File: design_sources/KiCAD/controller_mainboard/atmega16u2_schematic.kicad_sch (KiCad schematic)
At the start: 23 parts, among them J1 02x03_pinheader, J2 01x05_Socket, J3 02x02_pinheader, U2 ATmega16U2-M, Y2 16MHz

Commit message: Continued development on the schematic. Pins wired. TODO validate.
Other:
- company: Kestech -> Mete Han Keskin
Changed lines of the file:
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@@
 		(date "2025-03-01")
 		(rev "V1.0")
-		(company "Kestech")
-		(comment 1 "MIT License. Copyright (c) 2025 Kestech Fontys")
+		(company "Mete Han Keskin")
+		(comment 1 "MIT License. Copyright (c) 2025 kestech.net")
 	)
 	(text "02x02 SWD connector\n"

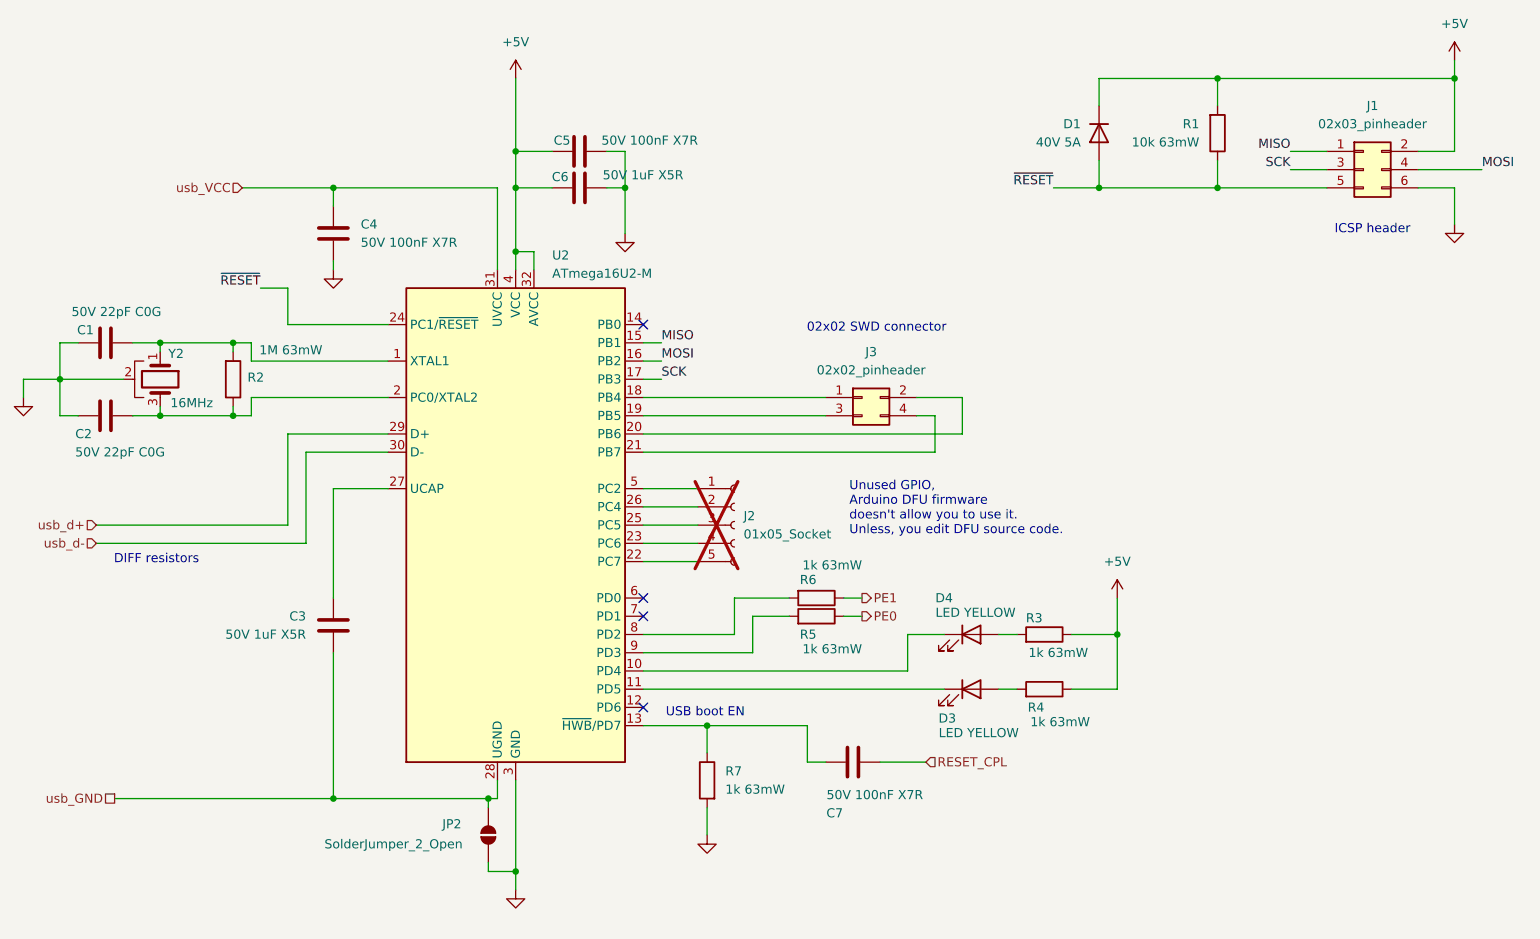
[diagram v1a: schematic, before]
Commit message: Added ESD protection ic, added footprints to all IC and loaded into pcbnew to size up the pcb size.
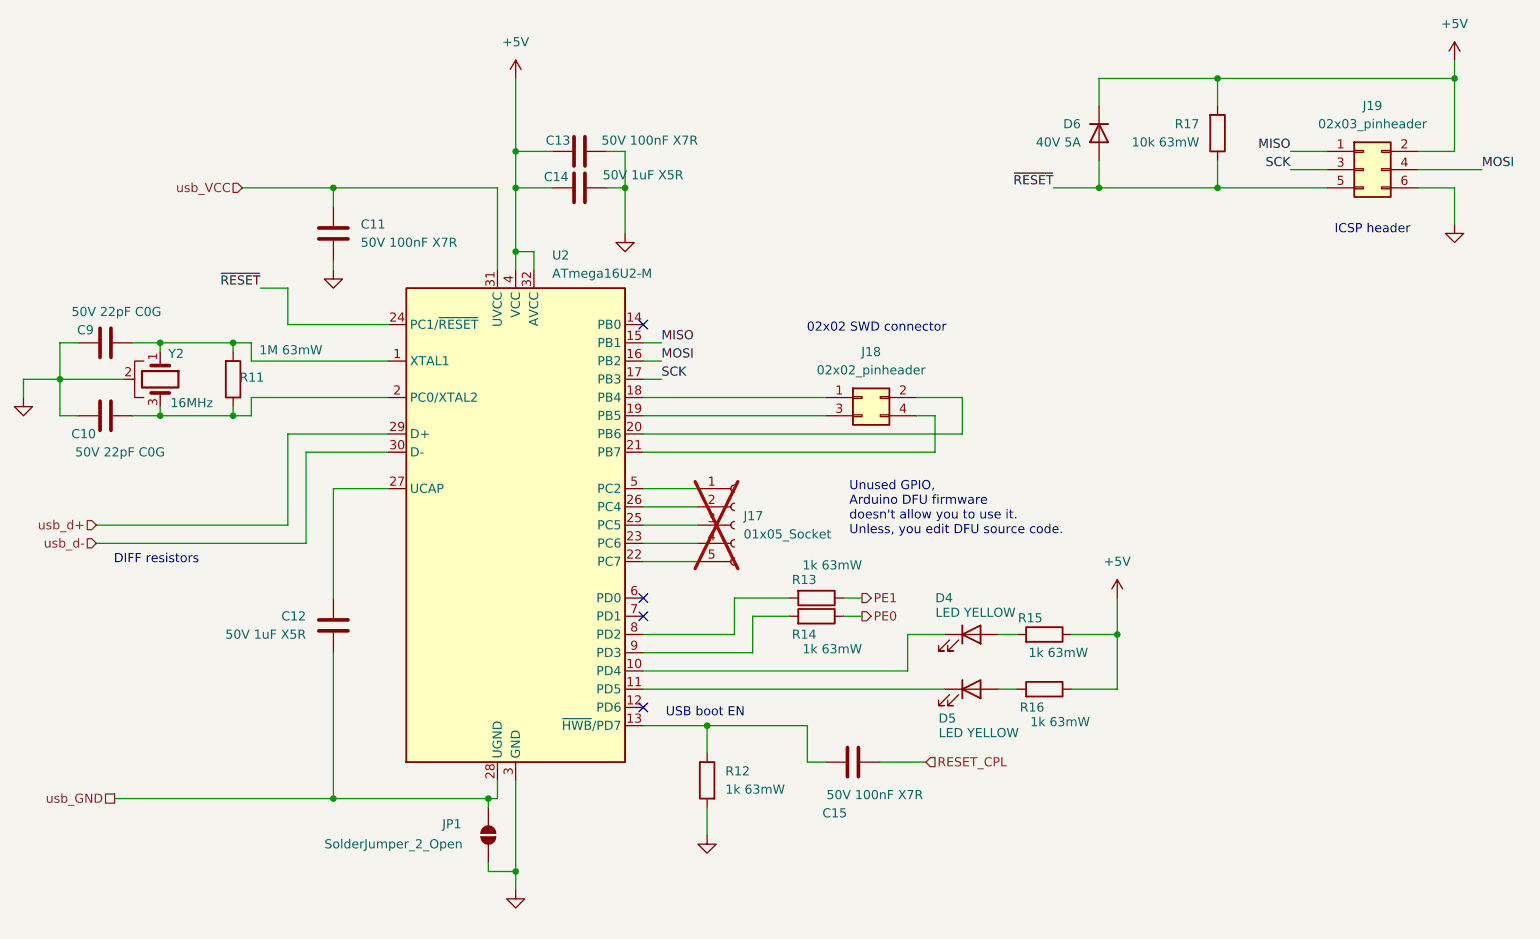
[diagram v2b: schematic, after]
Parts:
- J17: renamed from J2; footprint (none) -> Connector_PinSocket_2.54mm:PinSocket_1x05_P2.54mm_Vertical
- renumbered C2 to C10, C4 to C11, C3 to C12, C5 to C13, C6 to C14, C7 to C15, C1 to C9, D3 to D5, D1 to D6, J3 to J18, J1 to J19, JP2 to JP1, R2 to R11, R7 to R12, R6 to R13, R5 to R14, R3 to R15, R4 to R16, R1 to R17
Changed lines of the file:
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@@
 		(on_board yes)
 		(dnp no)
-		(property "Reference" "D1"
+		(property "Reference" "D6"
 			(at 180.34 43.1799 90)
 			(effects
@@
 			(project ""
 				(path "/0fdfffec-3d24-4249-8ba9-dae7a6ccc250/56a5a4f6-b055-4ffd-8e95-057054573d13"
-					(reference "D1")
+					(reference "D6")
 					(unit 1)
 				)
@@
 		(dnp no)
 		(fields_autoplaced yes)
-		(property "Reference" "C4"
+		(property "Reference" "C11"
 			(at 80.01 57.1499 0)
 			(effects
@@
 			(project ""
 				(path "/0fdfffec-3d24-4249-8ba9-dae7a6ccc250/56a5a4f6-b055-4ffd-8e95-057054573d13"
-					(reference "C4")
+					(reference "C11")
 					(unit 1)
 				)
@@
 		(dnp yes)
 		(fields_autoplaced yes)
-		(property "Reference" "J2"
+		(property "Reference" "J17"
 			(at 133.35 97.7899 0)
 			(effects
@@
 			)
 		)
-		(property "Footprint" ""
+		(property "Footprint" "Connector_PinSocket_2.54mm:PinSocket_1x05_P2.54mm_Vertical"
 			(at 132.08 99.06 0)
 			(effects
@@
 			(project ""
 				(path "/0fdfffec-3d24-4249-8ba9-dae7a6ccc250/56a5a4f6-b055-4ffd-8e95-057054573d13"
-					(reference "J2")
+					(reference "J17")
 					(unit 1)
 				)
@@
 		(on_board yes)
 		(dnp no)
-		(property "Reference" "R5"
+		(property "Reference" "R14"
 			(at 143.51 114.3 90)
 			(effects
@@
 			(project "controller_mainboard"
 				(path "/0fdfffec-3d24-4249-8ba9-dae7a6ccc250/56a5a4f6-b055-4ffd-8e95-057054573d13"
-					(reference "R5")
+					(reference "R14")
 					(unit 1)
 				)
@@
 		(dnp no)
 		(fields_autoplaced yes)
-		(property "Reference" "R7"
+		(property "Reference" "R12"
 			(at 130.81 133.3499 0)
 			(effects
@@
 			(project "controller_mainboard"
 				(path "/0fdfffec-3d24-4249-8ba9-dae7a6ccc250/56a5a4f6-b055-4ffd-8e95-057054573d13"
-					(reference "R7")
+					(reference "R12")
 					(unit 1)
 				)
@@
 		(dnp no)
 		(fields_autoplaced yes)
-		(property "Reference" "J3"
+		(property "Reference" "J18"
 			(at 151.13 74.93 0)
 			(effects
@@
 			(project ""
 				(path "/0fdfffec-3d24-4249-8ba9-dae7a6ccc250/56a5a4f6-b055-4ffd-8e95-057054573d13"
-					(reference "J3")
+					(reference "J18")
 					(unit 1)
 				)
@@
 		(dnp no)
 		(fields_autoplaced yes)
-		(property "Reference" "#PWR05"
+		(property "Reference" "#PWR053"
 			(at 76.2 69.85 0)
 			(effects
@@
 			(project ""
 				(path "/0fdfffec-3d24-4249-8ba9-dae7a6ccc250/56a5a4f6-b055-4ffd-8e95-057054573d13"
-					(reference "#PWR05")
+					(reference "#PWR053")
 					(unit 1)
 				)
@@
 		(on_board yes)
 		(dnp no)
-		(property "Reference" "D3"
+		(property "Reference" "D5"
 			(at 161.7345 125.984 0)
 			(effects
@@
 			(project "controller_mainboard"
 				(path "/0fdfffec-3d24-4249-8ba9-dae7a6ccc250/56a5a4f6-b055-4ffd-8e95-057054573d13"
-					(reference "D3")
+					(reference "D5")
 					(unit 1)
 				)
@@
 		(dnp no)
 		(fields_autoplaced yes)
-		(property "Reference" "#PWR07"
+		(property "Reference" "#PWR056"
 			(at 116.84 64.77 0)
 			(effects
@@
 			(project "controller_mainboard"
 				(path "/0fdfffec-3d24-4249-8ba9-dae7a6ccc250/56a5a4f6-b055-4ffd-8e95-057054573d13"
-					(reference "#PWR07")
+					(reference "#PWR056")
 					(unit 1)
 				)
@@
 		(dnp no)
 		(fields_autoplaced yes)
-		(property "Reference" "J1"
+		(property "Reference" "J19"
 			(at 220.98 40.64 0)
 			(effects
@@
 			(project ""
 				(path "/0fdfffec-3d24-4249-8ba9-dae7a6ccc250/56a5a4f6-b055-4ffd-8e95-057054573d13"
-					(reference "J1")
+					(reference "J19")
 					(unit 1)
 				)
@@
 		(dnp no)
 		(fields_autoplaced yes)
-		(property "Reference" "#PWR08"
+		(property "Reference" "#PWR058"
 			(at 185.42 113.03 0)
 			(effects
@@
 			(project "controller_mainboard"
 				(path "/0fdfffec-3d24-4249-8ba9-dae7a6ccc250/56a5a4f6-b055-4ffd-8e95-057054573d13"
-					(reference "#PWR08")
+					(reference "#PWR058")
 					(unit 1)
 				)
@@
 		(on_board yes)
 		(dnp no)
-		(property "Reference" "C5"
+		(property "Reference" "C13"
 			(at 109.22 45.466 90)
 			(effects
@@
 			(project "controller_mainboard"
 				(path "/0fdfffec-3d24-4249-8ba9-dae7a6ccc250/56a5a4f6-b055-4ffd-8e95-057054573d13"
-					(reference "C5")
+					(reference "C13")
 					(unit 1)
 				)
@@
 		(on_board yes)
 		(dnp no)
-		(property "Reference" "JP2"
+		(property "Reference" "JP1"
 			(at 92.71 140.716 90)
 			(effects
@@
 			(project "controller_mainboard"
 				(path "/0fdfffec-3d24-4249-8ba9-dae7a6ccc250/56a5a4f6-b055-4ffd-8e95-057054573d13"
-					(reference "JP2")
+					(reference "JP1")
 					(unit 1)
 				)
@@
 		(dnp no)
 		(fields_autoplaced yes)
-		(property "Reference" "#PWR01"
+		(property "Reference" "#PWR060"
 			(at 232.41 63.5 0)
 			(effects
@@
 			(project ""
 				(path "/0fdfffec-3d24-4249-8ba9-dae7a6ccc250/56a5a4f6-b055-4ffd-8e95-057054573d13"
-					(reference "#PWR01")
+					(reference "#PWR060")
 					(unit 1)
 				)
@@
 		(on_board yes)
 		(dnp no)
-		(property "Reference" "C1"
+		(property "Reference" "C9"
 			(at 41.656 71.882 90)
 			(effects
@@
 			(project ""
 				(path "/0fdfffec-3d24-4249-8ba9-dae7a6ccc250/56a5a4f6-b055-4ffd-8e95-057054573d13"
-					(reference "C1")
+					(reference "C9")
 					(unit 1)
 				)
@@
 		(dnp no)
 		(fields_autoplaced yes)
-		(property "Reference" "#PWR03"
+		(property "Reference" "#PWR052"
 			(at 33.02 87.63 0)
 			(effects
@@
 			(project ""
 				(path "/0fdfffec-3d24-4249-8ba9-dae7a6ccc250/56a5a4f6-b055-4ffd-8e95-057054573d13"
-					(reference "#PWR03")
+					(reference "#PWR052")
 					(unit 1)
 				)
@@
 		(on_board yes)
 		(dnp no)
-		(property "Reference" "C6"
+		(property "Reference" "C14"
 			(at 108.966 50.546 90)
 			(effects
@@
 			(project "controller_mainboard"
 				(path "/0fdfffec-3d24-4249-8ba9-dae7a6ccc250/56a5a4f6-b055-4ffd-8e95-057054573d13"
-					(reference "C6")
+					(reference "C14")
 					(unit 1)
 				)
@@
 		(on_board yes)
 		(dnp no)
-		(property "Reference" "C3"
+		(property "Reference" "C12"
 			(at 72.39 111.7599 0)
 			(effects
@@
 			(project ""
 				(path "/0fdfffec-3d24-4249-8ba9-dae7a6ccc250/56a5a4f6-b055-4ffd-8e95-057054573d13"
-					(reference "C3")
+					(reference "C12")
 					(unit 1)
 				)
@@
 		(on_board yes)
 		(dnp no)
-		(property "Reference" "R6"
+		(property "Reference" "R13"
 			(at 143.51 106.68 90)
 			(effects
@@
 			(project "controller_mainboard"
 				(path "/0fdfffec-3d24-4249-8ba9-dae7a6ccc250/56a5a4f6-b055-4ffd-8e95-057054573d13"
-					(reference "R6")
+					(reference "R13")
 					(unit 1)
 				)
@@
 		(on_board yes)
 		(dnp no)
-		(property "Reference" "C2"
+		(property "Reference" "C10"
 			(at 41.402 86.36 90)
 			(effects
@@
 			(project "controller_mainboard"
 				(path "/0fdfffec-3d24-4249-8ba9-dae7a6ccc250/56a5a4f6-b055-4ffd-8e95-057054573d13"
-					(reference "C2")
+					(reference "C10")
 					(unit 1)
 				)
@@
 		(on_board yes)
 		(dnp no)
-		(property "Reference" "R2"
+		(property "Reference" "R11"
 			(at 66.548 78.486 0)
 			(effects
@@
 			(project "controller_mainboard"
 				(path "/0fdfffec-3d24-4249-8ba9-dae7a6ccc250/56a5a4f6-b055-4ffd-8e95-057054573d13"
-					(reference "R2")
+					(reference "R11")
 					(unit 1)
 				)
@@
 		(dnp no)
 		(fields_autoplaced yes)
-		(property "Reference" "#PWR04"
+		(property "Reference" "#PWR055"
 			(at 101.6 156.21 0)
 			(effects
@@
 			(project ""
 				(path "/0fdfffec-3d24-4249-8ba9-dae7a6ccc250/56a5a4f6-b055-4ffd-8e95-057054573d13"
-					(reference "#PWR04")
+					(reference "#PWR055")
 					(unit 1)
 				)
@@
 		(dnp no)
 		(fields_autoplaced yes)
-		(property "Reference" "#PWR06"
+		(property "Reference" "#PWR054"
 			(at 101.6 40.64 0)
 			(effects
@@
 			(project ""
 				(path "/0fdfffec-3d24-4249-8ba9-dae7a6ccc250/56a5a4f6-b055-4ffd-8e95-057054573d13"
-					(reference "#PWR06")
+					(reference "#PWR054")
 					(unit 1)
 				)
@@
 		(on_board yes)
 		(dnp no)
-		(property "Reference" "R1"
+		(property "Reference" "R17"
 			(at 196.85 43.1799 0)
 			(effects
@@
 			(project ""
 				(path "/0fdfffec-3d24-4249-8ba9-dae7a6ccc250/56a5a4f6-b055-4ffd-8e95-057054573d13"
-					(reference "R1")
+					(reference "R17")
 					(unit 1)
 				)
@@
 		(dnp no)
 		(fields_autoplaced yes)
-		(property "Reference" "#PWR09"
+		(property "Reference" "#PWR057"
 			(at 128.27 148.59 0)
 			(effects
@@
 			(project "controller_mainboard"
 				(path "/0fdfffec-3d24-4249-8ba9-dae7a6ccc250/56a5a4f6-b055-4ffd-8e95-057054573d13"
-					(reference "#PWR09")
+					(reference "#PWR057")
 					(unit 1)
 				)
@@
 		(dnp no)
 		(fields_autoplaced yes)
-		(property "Reference" "#PWR02"
+		(property "Reference" "#PWR059"
 			(at 232.41 38.1 0)
 			(effects
@@
 			(project ""
 				(path "/0fdfffec-3d24-4249-8ba9-dae7a6ccc250/56a5a4f6-b055-4ffd-8e95-057054573d13"
-					(reference "#PWR02")
+					(reference "#PWR059")
 					(unit 1)
 				)
@@
 		(on_board yes)
 		(dnp no)
-		(property "Reference" "R3"
+		(property "Reference" "R15"
 			(at 175.006 112.014 90)
 			(effects
@@
 			(project "controller_mainboard"
 				(path "/0fdfffec-3d24-4249-8ba9-dae7a6ccc250/56a5a4f6-b055-4ffd-8e95-057054573d13"
-					(reference "R3")
+					(reference "R15")
 					(unit 1)
 				)
@@
 		(on_board yes)
 		(dnp no)
-		(property "Reference" "C7"
+		(property "Reference" "C15"
 			(at 146.05 139.192 90)
 			(effects
@@
 			(project "controller_mainboard"
 				(path "/0fdfffec-3d24-4249-8ba9-dae7a6ccc250/56a5a4f6-b055-4ffd-8e95-057054573d13"
-					(reference "C7")
+					(reference "C15")
 					(unit 1)
 				)
@@
 		(on_board yes)
 		(dnp no)
-		(property "Reference" "R4"
+		(property "Reference" "R16"
 			(at 175.26 124.46 90)
 			(effects
@@
 			(project "controller_mainboard"
 				(path "/0fdfffec-3d24-4249-8ba9-dae7a6ccc250/56a5a4f6-b055-4ffd-8e95-057054573d13"
-					(reference "R4")
-					(unit 1)
-				)
+					(reference "R16")
+					(unit 1)
+				)

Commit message: Read through schematic to bugfix.
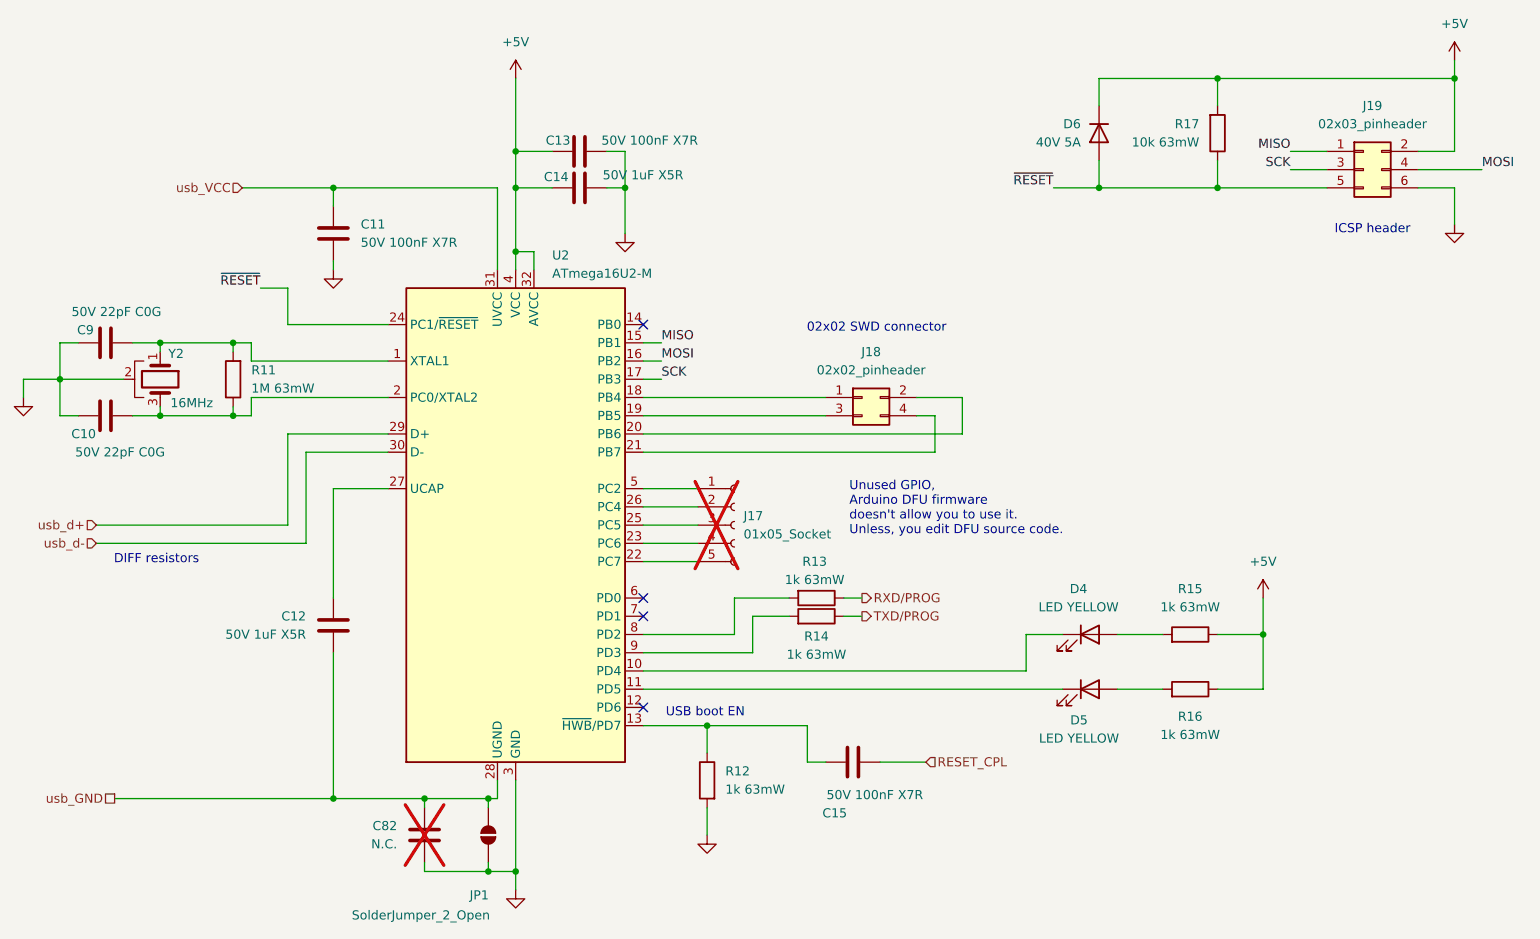
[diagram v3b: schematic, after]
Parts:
- added C82: N.C., Capacitor_SMD:C_0603_1608Metric, symbol Device:C
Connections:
- net GND: now also C82.1
- net usb_GND: now also C82.2
- net PE0 renamed TXD/PROG
- net PE1 renamed RXD/PROG
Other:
- moved on the sheet: D4, D5, R11, R15, R16

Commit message: Adjusted gitignore to ignore backups, removed backup files
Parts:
- J18: footprint (none) -> Connector_PinHeader_2.54mm:PinHeader_2x02_P2.54mm_Vertical
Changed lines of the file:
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@@
 			)
 		)
-		(property "Footprint" ""
+		(property "Footprint" "Connector_PinHeader_2.54mm:PinHeader_2x02_P2.54mm_Vertical"
 			(at 149.86 81.28 0)
 			(effects
